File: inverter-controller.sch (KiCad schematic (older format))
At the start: 0 parts

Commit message: Adds todos.
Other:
- note added: "TODO(willjschmitt): Add precharge relay."
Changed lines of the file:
@@
 Text Notes 4650 4350 0    60   ~ 0
 Hardware Fault Handling
+Text Notes 8150 4350 0    60   ~ 0
+TODO(willjschmitt): Add precharge relay.
 $EndSCHEMATC

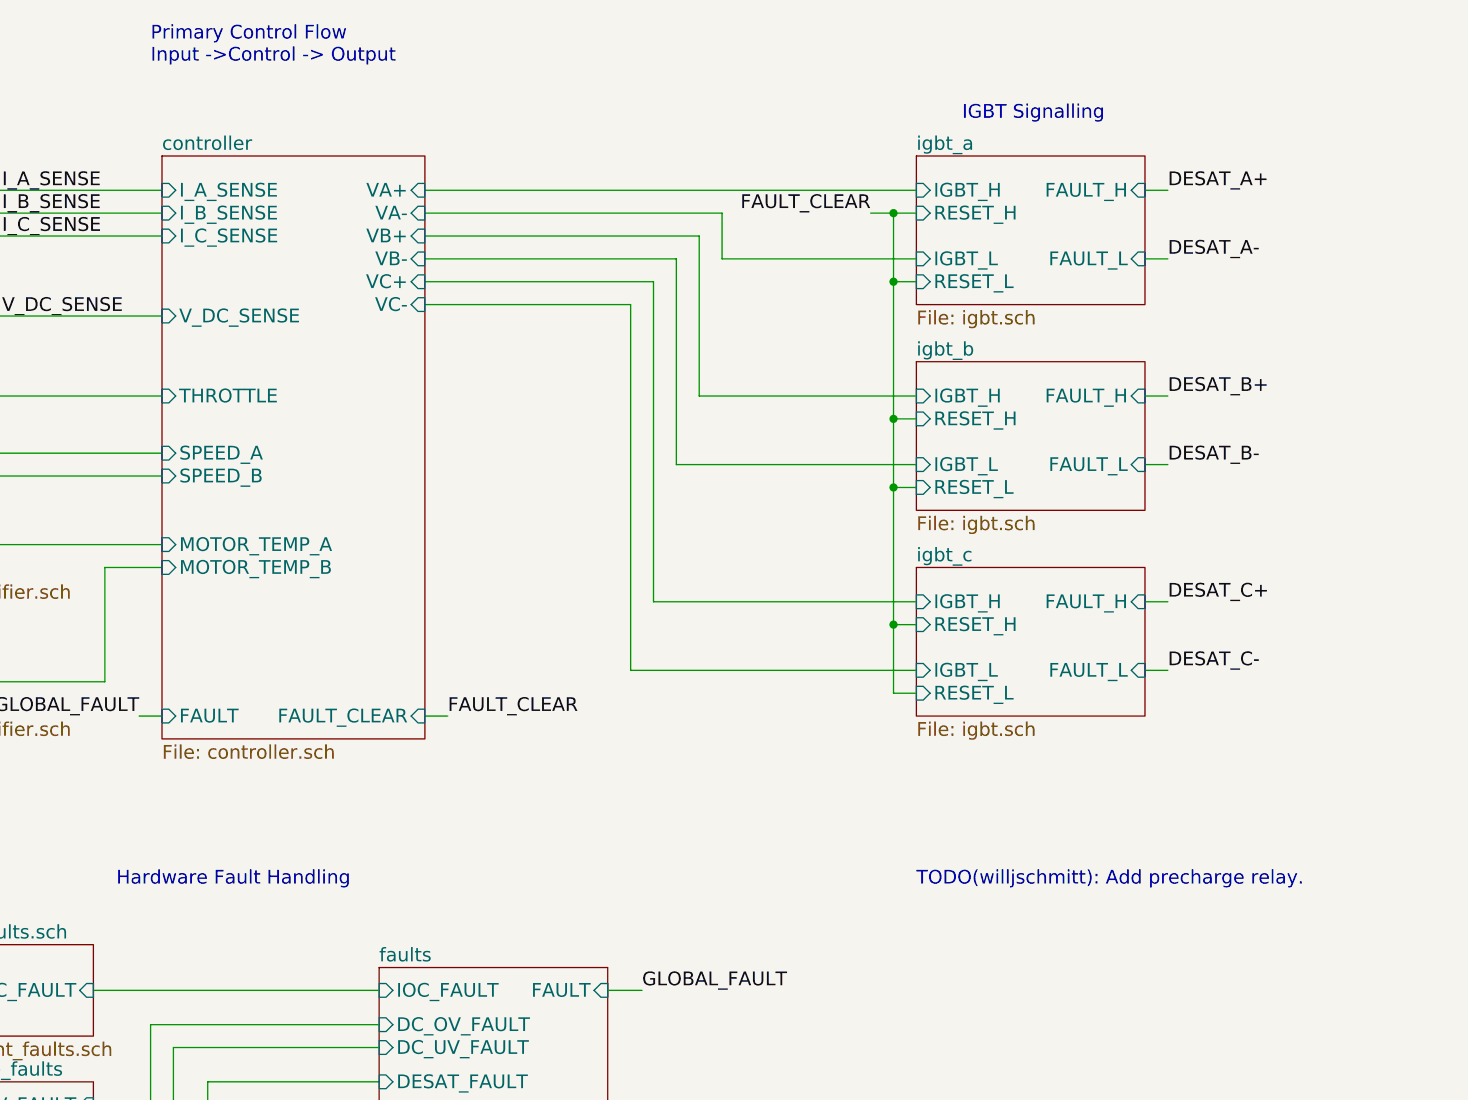
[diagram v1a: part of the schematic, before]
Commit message: Adding contactor placeholders.
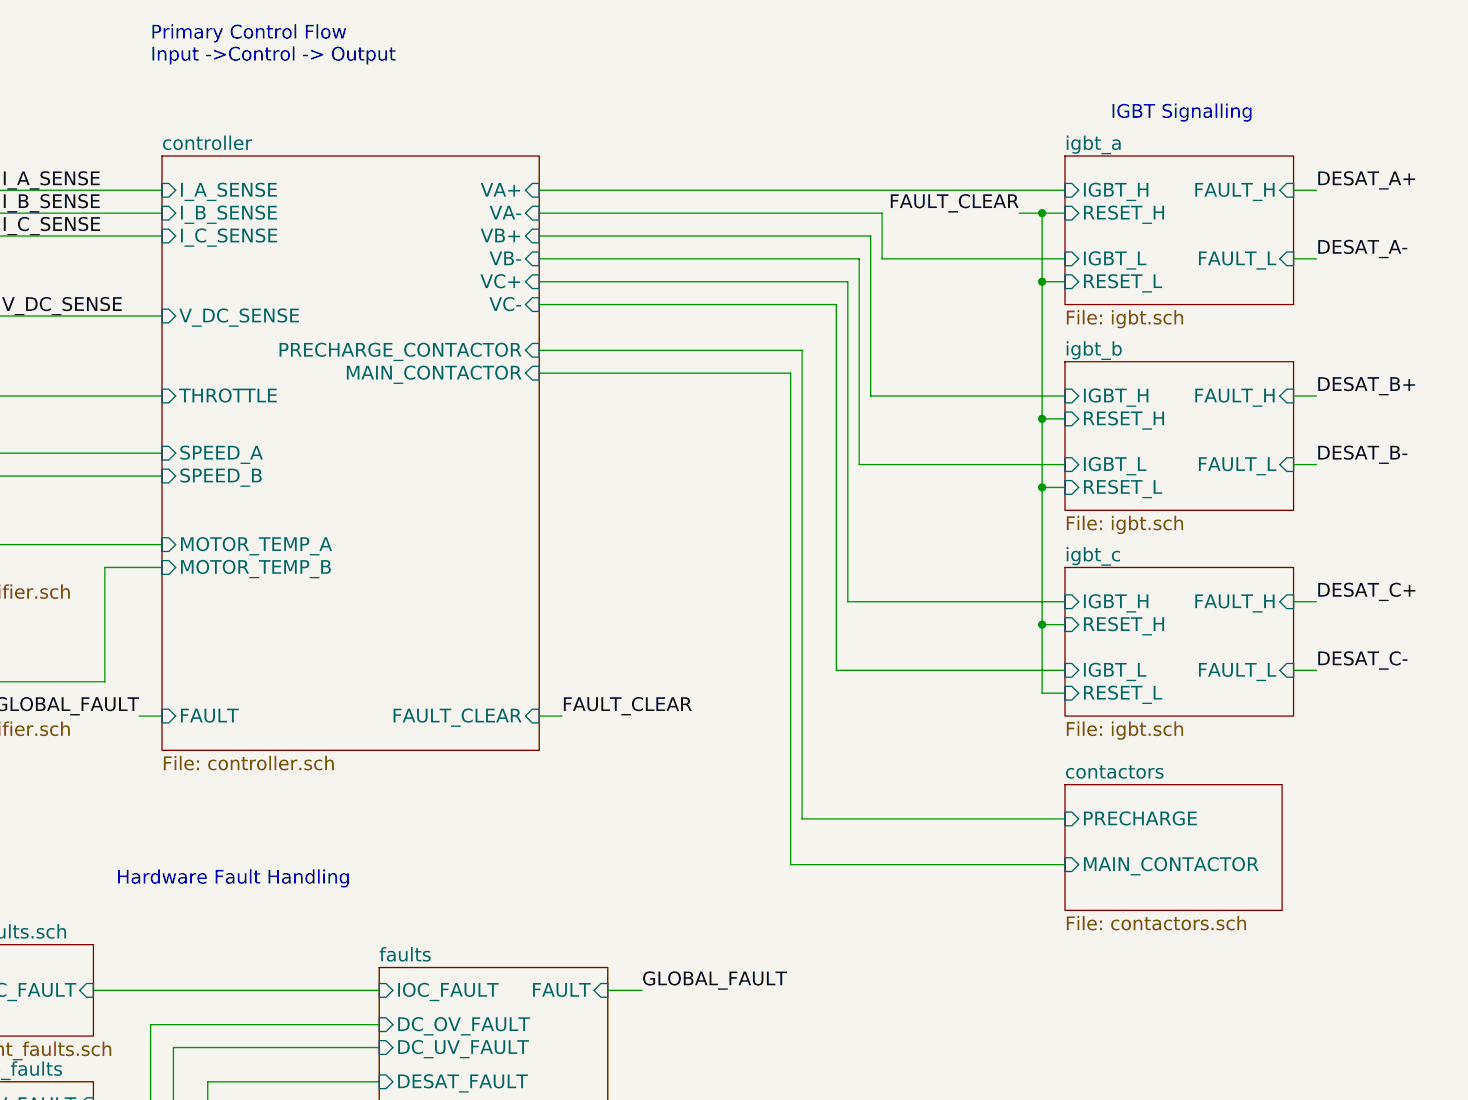
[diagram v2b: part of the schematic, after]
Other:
- note removed: "TODO(willjschmitt): Add precharge relay."
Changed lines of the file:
@@
 $Descr A4 11693 8268
 encoding utf-8
-Sheet 1 15
+Sheet 1 18
 Title ""
 Date ""
@@
 $EndDescr
 $Sheet
-S 4850 1150 1150 2550
+S 4850 1150 1650 2600
 U 5AEC1F05
 F0 "controller" 60
 F1 "controller.sch" 60
-F2 "VB-" I R 6000 1600 60
-F3 "VB+" I R 6000 1500 60
-F4 "VC-" I R 6000 1800 60
-F5 "VC+" I R 6000 1700 60
-F6 "VA+" I R 6000 1300 60
-F7 "VA-" I R 6000 1400 60
+F2 "VB-" I R 6500 1600 60
+F3 "VB+" I R 6500 1500 60
+F4 "VC-" I R 6500 1800 60
+F5 "VC+" I R 6500 1700 60
+F6 "VA+" I R 6500 1300 60
+F7 "VA-" I R 6500 1400 60
 F8 "I_A_SENSE" I L 4850 1300 60
 F9 "I_B_SENSE" I L 4850 1400 60
@@
 F12 "THROTTLE" I L 4850 2200 60
 F13 "FAULT" I L 4850 3600 60
-F14 "FAULT_CLEAR" I R 6000 3600 60
+F14 "FAULT_CLEAR" I R 6500 3600 60
 F15 "SPEED_A" I L 4850 2450 60
 F16 "SPEED_B" I L 4850 2550 60
 F17 "MOTOR_TEMP_A" I L 4850 2850 60
 F18 "MOTOR_TEMP_B" I L 4850 2950 60
-$EndSheet
-$Sheet
-S 8150 1150 1000 650
+F19 "PRECHARGE_CONTACTOR" I R 6500 2000 60
+F20 "MAIN_CONTACTOR" I R 6500 2100 60
+$EndSheet
+$Sheet
+S 8800 1150 1000 650
 U 5AED5DDF
 F0 "igbt_a" 60
 F1 "igbt.sch" 60
-F2 "IGBT_H" I L 8150 1300 60
-F3 "IGBT_L" I L 8150 1600 60
-F4 "FAULT_H" I R 9150 1300 60
-F5 "RESET_H" I L 8150 1400 60
-F6 "FAULT_L" I R 9150 1600 60
-F7 "RESET_L" I L 8150 1700 60
-$EndSheet
-$Sheet
-S 8150 2050 1000 650
+F2 "IGBT_H" I L 8800 1300 60
+F3 "IGBT_L" I L 8800 1600 60
+F4 "FAULT_H" I R 9800 1300 60
+F5 "RESET_H" I L 8800 1400 60
+F6 "FAULT_L" I R 9800 1600 60
+F7 "RESET_L" I L 8800 1700 60
+$EndSheet
+$Sheet
+S 8800 2050 1000 650
 U 5AEDA321
 F0 "igbt_b" 60
 F1 "igbt.sch" 60
-F2 "IGBT_H" I L 8150 2200 60
-F3 "IGBT_L" I L 8150 2500 60
-F4 "FAULT_H" I R 9150 2200 60
-F5 "RESET_H" I L 8150 2300 60
-F6 "FAULT_L" I R 9150 2500 60
-F7 "RESET_L" I L 8150 2600 60
-$EndSheet
-$Sheet
-S 8150 2950 1000 650
+F2 "IGBT_H" I L 8800 2200 60
+F3 "IGBT_L" I L 8800 2500 60
+F4 "FAULT_H" I R 9800 2200 60
+F5 "RESET_H" I L 8800 2300 60
+F6 "FAULT_L" I R 9800 2500 60
+F7 "RESET_L" I L 8800 2600 60
+$EndSheet
+$Sheet
+S 8800 2950 1000 650
 U 5AEDAF6D
 F0 "igbt_c" 60
 F1 "igbt.sch" 60
-F2 "IGBT_H" I L 8150 3100 60
-F3 "IGBT_L" I L 8150 3400 60
-F4 "FAULT_H" I R 9150 3100 60
-F5 "RESET_H" I L 8150 3200 60
-F6 "FAULT_L" I R 9150 3400 60
-F7 "RESET_L" I L 8150 3500 60
+F2 "IGBT_H" I L 8800 3100 60
+F3 "IGBT_L" I L 8800 3400 60
+F4 "FAULT_H" I R 9800 3100 60
+F5 "RESET_H" I L 8800 3200 60
+F6 "FAULT_L" I R 9800 3400 60
+F7 "RESET_L" I L 8800 3500 60
 $EndSheet
 $Sheet
@@
 	2600 1500 4850 1500
 Wire Wire Line
-	6000 1300 8150 1300
-Wire Wire Line
-	7300 1600 8150 1600
-Wire Wire Line
-	6000 1500 7200 1500
-Wire Wire Line
-	6000 1700 7000 1700
-Wire Wire Line
-	6000 1800 6900 1800
-Wire Wire Line
-	7200 2200 8150 2200
-Wire Wire Line
-	7100 2500 8150 2500
-Wire Wire Line
-	7000 3100 8150 3100
+	6500 1300 8800 1300
+Wire Wire Line
+	8000 1600 8800 1600
+Wire Wire Line
+	6500 1500 7950 1500
+Wire Wire Line
+	6500 1700 7850 1700
+Wire Wire Line
+	6500 1800 7800 1800
+Wire Wire Line
+	7950 2200 8800 2200
+Wire Wire Line
+	7900 2500 8800 2500
+Wire Wire Line
+	7850 3100 8800 3100
 Wire Wire Line
 	4850 1850 2600 1850
 Wire Wire Line
-	7300 1400 7300 1600
-Wire Wire Line
-	7200 1500 7200 2200
-Wire Wire Line
-	7100 1600 7100 2500
-Wire Wire Line
-	7000 1700 7000 3100
-Wire Wire Line
-	6900 1800 6900 3400
-Wire Wire Line
-	6900 3400 8150 3400
+	8000 1400 8000 1600
+Wire Wire Line
+	7950 1500 7950 2200
+Wire Wire Line
+	7900 1600 7900 2500
+Wire Wire Line
+	7850 1700 7850 3100
+Wire Wire Line
+	7800 1800 7800 3400
+Wire Wire Line
+	7800 3400 8800 3400
 Wire Wire Line
 	2600 2200 4850 2200
 Wire Wire Line
-	6000 1400 7300 1400
-Wire Wire Line
-	6000 1600 7100 1600
+	6500 1400 8000 1400
+Wire Wire Line
+	6500 1600 7900 1600
 $Sheet
 S 3500 5850 1250 800
@@
 Text Label 5700 5600 2    60   ~ 0
 FAULT_CLEAR
-Text Label 6100 3600 0    60   ~ 0
+Text Label 6600 3600 0    60   ~ 0
 FAULT_CLEAR
 Text Label 4750 3600 2    60   ~ 0
@@
 	4750 3600 4850 3600
 Wire Wire Line
-	6100 3600 6000 3600
+	6600 3600 6500 3600
 $Sheet
 S 3450 2700 550  300
@@
 Wire Wire Line
 	4600 2950 4850 2950
-Text Label 9250 1300 0    60   ~ 0
+Text Label 9900 1300 0    60   ~ 0
 DESAT_A+
-Text Label 9250 1600 0    60   ~ 0
+Text Label 9900 1600 0    60   ~ 0
 DESAT_A-
-Text Label 9250 2200 0    60   ~ 0
+Text Label 9900 2200 0    60   ~ 0
 DESAT_B+
-Text Label 9250 2500 0    60   ~ 0
+Text Label 9900 2500 0    60   ~ 0
 DESAT_B-
-Text Label 9250 3100 0    60   ~ 0
+Text Label 9900 3100 0    60   ~ 0
 DESAT_C+
-Text Label 9250 3400 0    60   ~ 0
+Text Label 9900 3400 0    60   ~ 0
 DESAT_C-
 Wire Wire Line
-	9250 1300 9150 1300
-Wire Wire Line
-	9150 1600 9250 1600
-Wire Wire Line
-	9150 2200 9250 2200
-Wire Wire Line
-	9250 2500 9150 2500
-Wire Wire Line
-	9150 3100 9250 3100
-Wire Wire Line
-	9250 3400 9150 3400
+	9900 1300 9800 1300
+Wire Wire Line
+	9800 1600 9900 1600
+Wire Wire Line
+	9800 2200 9900 2200
+Wire Wire Line
+	9900 2500 9800 2500
+Wire Wire Line
+	9800 3100 9900 3100
+Wire Wire Line
+	9900 3400 9800 3400
 Text Label 4150 1850 0    60   ~ 0
 V_DC_SENSE
@@
 Wire Wire Line
 	3400 6550 3500 6550
-Text Label 7950 1400 2    60   ~ 0
+Text Label 8600 1400 2    60   ~ 0
 FAULT_CLEAR
 Wire Wire Line
-	7950 1400 8150 1400
-Wire Wire Line
-	8050 1400 8050 3500
-Wire Wire Line
-	8050 3500 8150 3500
-Wire Wire Line
-	8150 3200 8050 3200
-Connection ~ 8050 3200
-Wire Wire Line
-	8150 2600 8050 2600
-Connection ~ 8050 2600
-Wire Wire Line
-	8150 2300 8050 2300
-Connection ~ 8050 2300
-Wire Wire Line
-	8150 1700 8050 1700
-Connection ~ 8050 1700
-Connection ~ 8050 1400
+	8600 1400 8800 1400
+Wire Wire Line
+	8700 1400 8700 3500
+Wire Wire Line
+	8700 3500 8800 3500
+Wire Wire Line
+	8800 3200 8700 3200
+Connection ~ 8700 3200
+Wire Wire Line
+	8800 2600 8700 2600
+Connection ~ 8700 2600
+Wire Wire Line
+	8800 2300 8700 2300
+Connection ~ 8700 2300
+Wire Wire Line
+	8800 1700 8700 1700
+Connection ~ 8700 1700
+Connection ~ 8700 1400
 Text Notes 4800 750  0    60   ~ 0
 Primary Control Flow\nInput ->Control -> Output
 Text Notes 1850 1050 0    60   ~ 0
 Data Acquisition
-Text Notes 8350 1000 0    60   ~ 0
+Text Notes 9000 1000 0    60   ~ 0
 IGBT Signalling
 Text Notes 4650 4350 0    60   ~ 0
 Hardware Fault Handling
-Text Notes 8150 4350 0    60   ~ 0
-TODO(willjschmitt): Add precharge relay.
+$Sheet
+S 8800 3900 950  550
+U 5AFF2F49
+F0 "contactors" 60
+F1 "contactors.sch" 60
+F2 "PRECHARGE" I L 8800 4050 60
+F3 "MAIN_CONTACTOR" I L 8800 4250 60
+$EndSheet
+Wire Wire Line
+	6500 2000 7650 2000
+Wire Wire Line
+	7650 2000 7650 4050
+Wire Wire Line
+	7650 4050 8800 4050
+Wire Wire Line
+	6500 2100 7600 2100
+Wire Wire Line
+	7600 2100 7600 4250
+Wire Wire Line
+	7600 4250 8800 4250
 $EndSCHEMATC

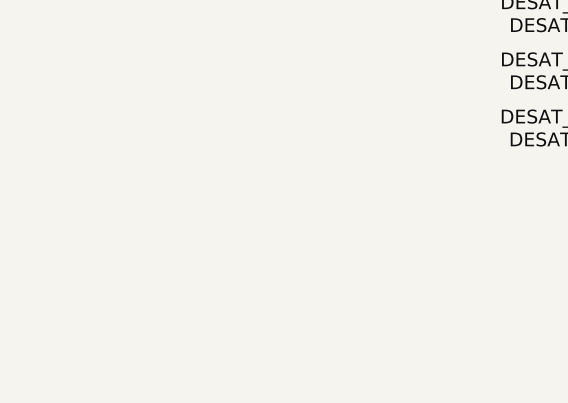
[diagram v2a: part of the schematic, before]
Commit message: Implement temperature sensor amplifier.
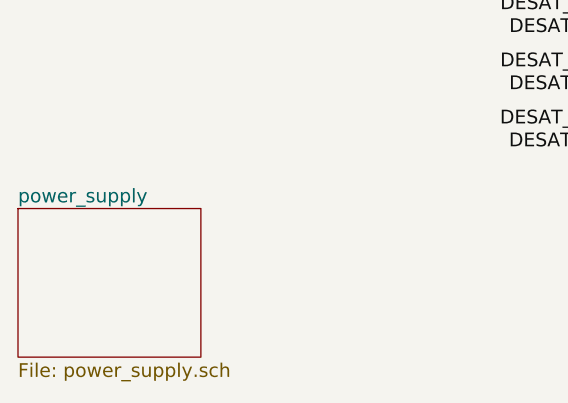
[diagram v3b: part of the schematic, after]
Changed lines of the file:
@@
 $Descr A4 11693 8268
 encoding utf-8
-Sheet 1 18
+Sheet 1 19
 Title ""
 Date ""
@@
 Wire Wire Line
 	7600 4250 8800 4250
+$Sheet
+S 850  6800 800  650
+U 5B0139C6
+F0 "power_supply" 60
+F1 "power_supply.sch" 60
+$EndSheet
 $EndSCHEMATC

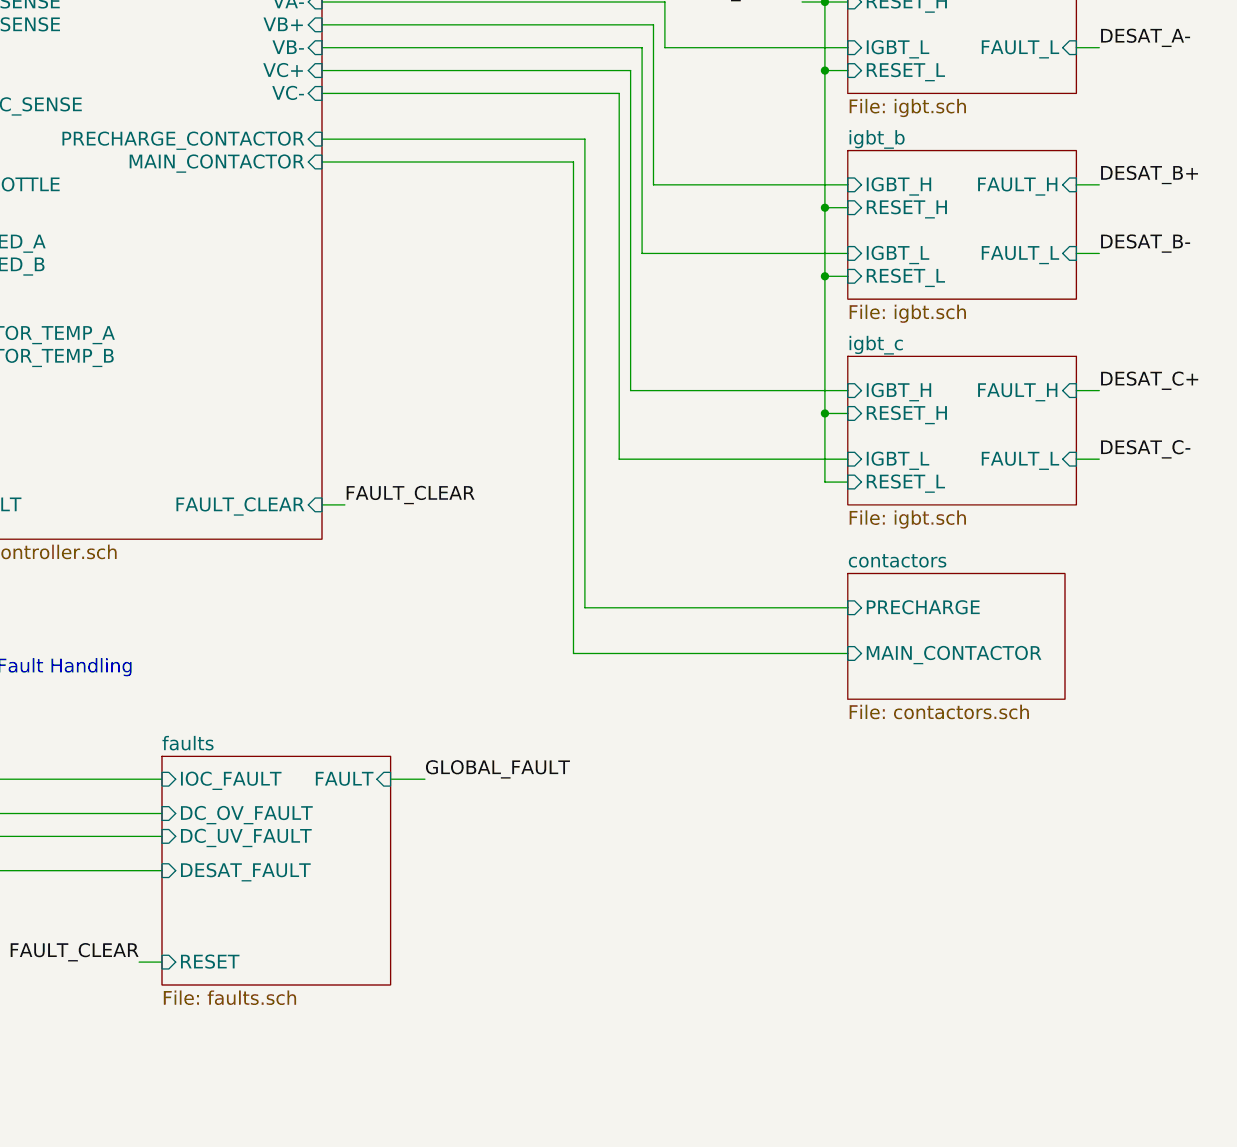
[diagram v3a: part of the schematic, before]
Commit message: Add fault lockout to relays.
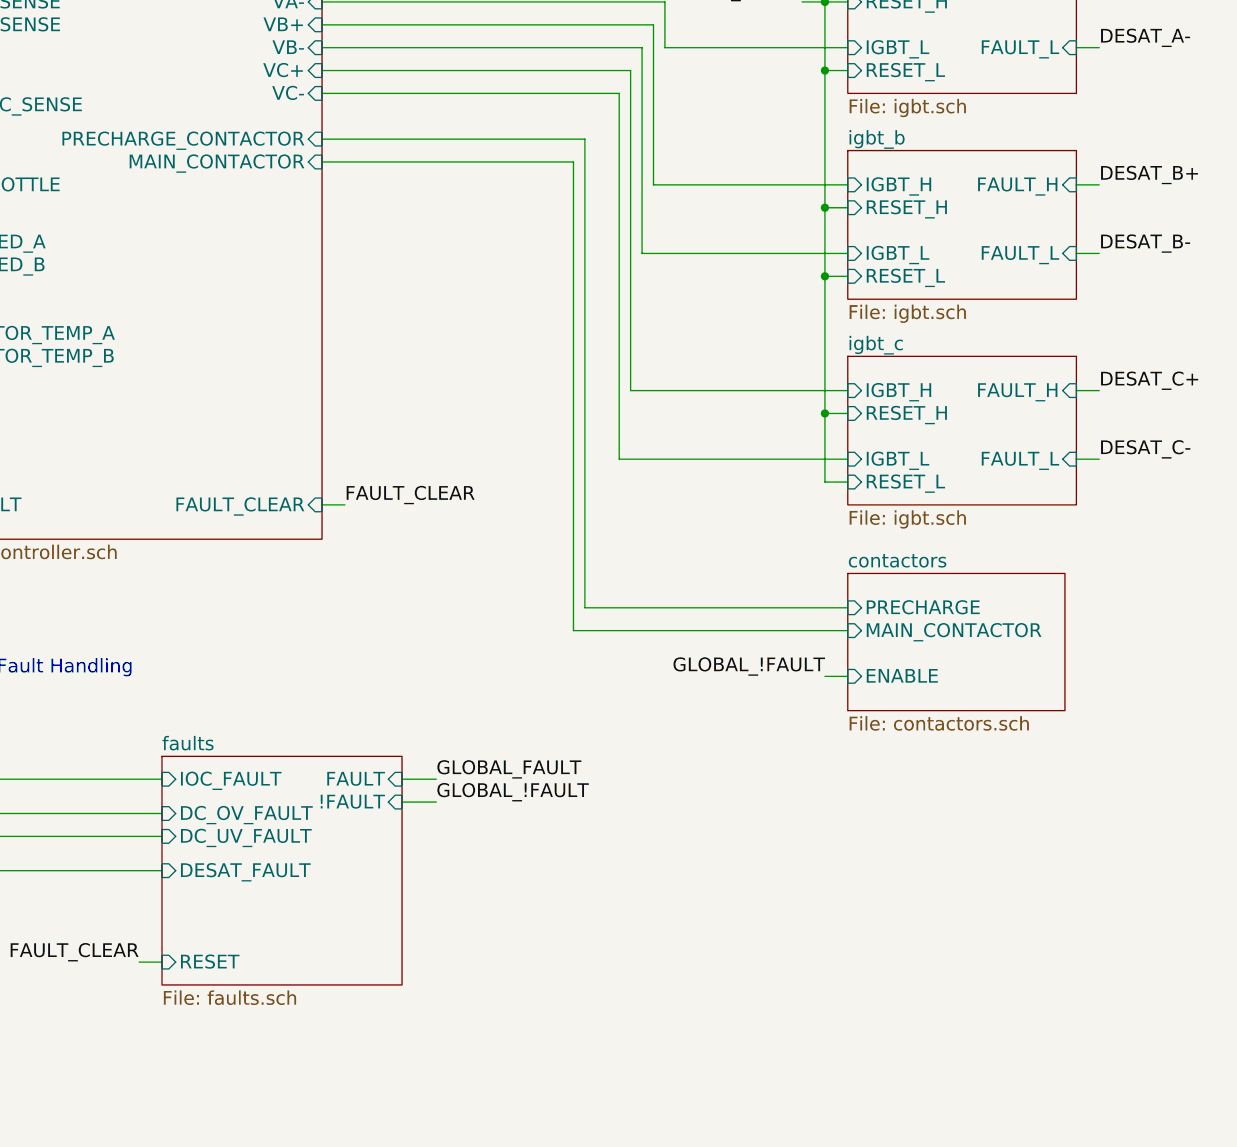
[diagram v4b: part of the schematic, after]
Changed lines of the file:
@@
 	3550 4900 3700 4900
 $Sheet
-S 5800 4700 1000 1000
+S 5800 4700 1050 1000
 U 5AF2FEC4
 F0 "faults" 60
@@
 F3 "DESAT_FAULT" I L 5800 5200 60
 F4 "RESET" I L 5800 5600 60
-F5 "FAULT" I R 6800 4800 60
+F5 "FAULT" I R 6850 4800 60
 F6 "DC_OV_FAULT" I L 5800 4950 60
 F7 "DC_UV_FAULT" I L 5800 5050 60
+F8 "!FAULT" I R 6850 4900 60
 $EndSheet
 Wire Wire Line
@@
 	5700 5600 5800 5600
 Wire Wire Line
-	6800 4800 6950 4800
-Text Label 6950 4800 0    60   ~ 0
+	6850 4800 7000 4800
+Text Label 7000 4800 0    60   ~ 0
 GLOBAL_FAULT
 Text Label 5700 5600 2    60   ~ 0
@@
 Hardware Fault Handling
 $Sheet
-S 8800 3900 950  550
+S 8800 3900 950  600
 U 5AFF2F49
 F0 "contactors" 60
 F1 "contactors.sch" 60
 F2 "PRECHARGE" I L 8800 4050 60
-F3 "MAIN_CONTACTOR" I L 8800 4250 60
+F3 "MAIN_CONTACTOR" I L 8800 4150 60
+F4 "ENABLE" I L 8800 4350 60
 $EndSheet
 Wire Wire Line
@@
 	6500 2100 7600 2100
 Wire Wire Line
-	7600 2100 7600 4250
-Wire Wire Line
-	7600 4250 8800 4250
+	7600 2100 7600 4150
+Wire Wire Line
+	7600 4150 8800 4150
 $Sheet
 S 850  6800 800  650
@@
 F1 "power_supply.sch" 60
 $EndSheet
+Text Label 7000 4900 0    60   ~ 0
+GLOBAL_!FAULT
+Wire Wire Line
+	7000 4900 6850 4900
+Text Label 8700 4350 2    60   ~ 0
+GLOBAL_!FAULT
+Wire Wire Line
+	8700 4350 8800 4350
 $EndSCHEMATC
